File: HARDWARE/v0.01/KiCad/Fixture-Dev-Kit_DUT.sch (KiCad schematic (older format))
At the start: 33 parts, among them J34 Conn_01x20, J35 BAT, J36 CHIP4LH, J37 USB_OTG, J38 Conn_01x20, J39 VBUS, J40 VBUS, J41 B_D+, J42 D-TP's, J43 B_D-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

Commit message: adding datasheets
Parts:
- D13: value LED -> LNJP12X8ARA
- SW9: value SW_Push -> TL9210AF260Q
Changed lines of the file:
@@
 P 950 5250
 F 0 "SW9" H 1000 5350 50  0000 L CNN
-F 1 "SW_Push" H 950 5190 50  0000 C CNN
+F 1 "TL9210AF260Q" H 950 5190 50  0000 C CNN
 F 2 "" H 950 5450 50  0001 C CNN
 F 3 "" H 950 5450 50  0001 C CNN
@@
 P 2900 7200
 F 0 "D13" H 2900 7300 50  0000 C CNN
-F 1 "LED" H 2900 7100 50  0000 C CNN
+F 1 "LNJP12X8ARA" H 2900 7100 50  0000 C CNN
 F 2 "LEDs:LED_0805_HandSoldering" H 2900 7200 50  0001 C CNN
 F 3 "" H 2900 7200 50  0001 C CNN

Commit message: beginning pcb layout
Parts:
- added F2: 1206SFP300F, Fuse_Holders_and_Fuses:Fuse_SMD1206_HandSoldering, symbol Fuse
- added SW12: YSS-19-1202-N, symbol SW_Push_SPDT
- J36: footprint Pin_Headers:Pin_Header_Angled_2x20_Pitch2.54mm -> Pin_Headers:Pin_Header_Straight_2x20_Pitch2.54mm
- J52: footprint (none) -> Pin_Headers:Pin_Header_Straight_2x20_Pitch2.54mm
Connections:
- net DUT-CHG-IN: now reaches J36.2 (CHG-IN), J38.1 (Pin_1)
- net DUT-CHG-IN: now also J55.61 (USB_VBUS), J55.63 (USB_VBUS), J55.65 (USB_VBUS), J55.67 (USB_VBUS), J55.69 (USB_VBUS), J56.31 (Pin_31), J56.32 (Pin_32), J56.33 (Pin_33), J56.34 (Pin_34), J56.35 (Pin_35), F2.2
- new net: F2.1, SW12.3 (C)
- new net +5V: SW12.2 (B)
- no-connect marks 0 -> 1
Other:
- note added: "DUT-PWR\n"
- note added: "Sheet Connections"
- moved on the sheet: J42, J45, J46
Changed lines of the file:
@@
 $EndComp
 $Comp
-L GND #PWR043
+L GND #PWR047
 U 1 1 59EE39D0
 P 6700 4200
-F 0 "#PWR043" H 6700 3950 50  0001 C CNN
+F 0 "#PWR047" H 6700 3950 50  0001 C CNN
 F 1 "GND" H 6700 4050 50  0000 C CNN
 F 2 "" H 6700 4200 50  0001 C CNN
@@
 $EndComp
 $Comp
-L GND #PWR044
+L GND #PWR048
 U 1 1 59EE3CBF
 P 2850 4300
-F 0 "#PWR044" H 2850 4050 50  0001 C CNN
+F 0 "#PWR048" H 2850 4050 50  0001 C CNN
 F 1 "GND" H 2850 4150 50  0000 C CNN
 F 2 "" H 2850 4300 50  0001 C CNN
@@
 D-PWRON_SW
 $Comp
-L GND #PWR045
+L GND #PWR049
 U 1 1 59EE44BA
 P 950 5550
-F 0 "#PWR045" H 950 5300 50  0001 C CNN
+F 0 "#PWR049" H 950 5300 50  0001 C CNN
 F 1 "GND" H 950 5400 50  0000 C CNN
 F 2 "" H 950 5550 50  0001 C CNN
@@
 $EndComp
 $Comp
-L GND #PWR046
+L GND #PWR050
 U 1 1 59EE4976
 P 1400 6400
-F 0 "#PWR046" H 1400 6150 50  0001 C CNN
+F 0 "#PWR050" H 1400 6150 50  0001 C CNN
 F 1 "GND" H 1400 6250 50  0000 C CNN
 F 2 "" H 1400 6400 50  0001 C CNN
@@
 $EndComp
 $Comp
-L GND #PWR047
+L GND #PWR051
 U 1 1 59EE8E82
 P 7550 6100
-F 0 "#PWR047" H 7550 5850 50  0001 C CNN
+F 0 "#PWR051" H 7550 5850 50  0001 C CNN
 F 1 "GND" H 7550 5950 50  0000 C CNN
 F 2 "" H 7550 6100 50  0001 C CNN
@@
 $EndComp
 $Comp
-L GND #PWR048
+L GND #PWR052
 U 1 1 59EE9E75
 P 7550 2350
-F 0 "#PWR048" H 7550 2100 50  0001 C CNN
+F 0 "#PWR052" H 7550 2100 50  0001 C CNN
 F 1 "GND" H 7550 2200 50  0000 C CNN
 F 2 "" H 7550 2350 50  0001 C CNN
@@
 D-TS
 $Comp
-L GND #PWR049
+L GND #PWR053
 U 1 1 59EEAB1E
 P 1250 7500
-F 0 "#PWR049" H 1250 7250 50  0001 C CNN
+F 0 "#PWR053" H 1250 7250 50  0001 C CNN
 F 1 "GND" H 1250 7350 50  0000 C CNN
 F 2 "" H 1250 7500 50  0001 C CNN
@@
 $EndComp
 $Comp
-L GND #PWR050
+L GND #PWR054
 U 1 1 59EEBA3C
 P 2900 7450
-F 0 "#PWR050" H 2900 7200 50  0001 C CNN
+F 0 "#PWR054" H 2900 7200 50  0001 C CNN
 F 1 "GND" H 2900 7300 50  0000 C CNN
 F 2 "" H 2900 7450 50  0001 C CNN
@@
 F 0 "J36" H 1150 6250 60  0000 C CNN
 F 1 "CHIP4LH" H 1500 3900 60  0000 C CNN
-F 2 "Pin_Headers:Pin_Header_Angled_2x20_Pitch2.54mm" H 1800 4050 60  0001 C CNN
+F 2 "Pin_Headers:Pin_Header_Straight_2x20_Pitch2.54mm" H 1800 4050 60  0001 C CNN
 F 3 "" H 1800 4050 60  0001 C CNN
 	1    1700 4050
@@
 F 0 "J52" H 5050 6000 60  0000 C CNN
 F 1 "CHIP4RH" H 5300 3850 60  0000 C CNN
-F 2 "" H 5600 3950 60  0001 C CNN
+F 2 "Pin_Headers:Pin_Header_Straight_2x20_Pitch2.54mm" H 5600 3950 60  0001 C CNN
 F 3 "" H 5600 3950 60  0001 C CNN
 	1    5550 3950
@@
 $EndComp
 $Comp
-L GND #PWR051
+L GND #PWR055
 U 1 1 59EE623C
 P 2500 6050
-F 0 "#PWR051" H 2500 5800 50  0001 C CNN
+F 0 "#PWR055" H 2500 5800 50  0001 C CNN
 F 1 "GND" H 2500 5900 50  0000 C CNN
 F 2 "" H 2500 6050 50  0001 C CNN
@@
 $EndComp
 $Comp
-L GND #PWR052
+L GND #PWR056
 U 1 1 59EE91D1
 P 4650 6050
-F 0 "#PWR052" H 4650 5800 50  0001 C CNN
+F 0 "#PWR056" H 4650 5800 50  0001 C CNN
 F 1 "GND" H 4650 5900 50  0000 C CNN
 F 2 "" H 4650 6050 50  0001 C CNN
@@
 L Conn_01x01 J45
 U 1 1 59EEA0FF
-P 4450 6750
-F 0 "J45" H 4450 6850 50  0000 C CNN
-F 1 "UPDATE" H 4450 6650 50  0000 C CNN
-F 2 "Pin_Headers:Pin_Header_Angled_1x01_Pitch2.54mm" H 4450 6750 50  0001 C CNN
-F 3 "" H 4450 6750 50  0001 C CNN
-	1    4450 6750
+P 4400 6750
+F 0 "J45" H 4400 6850 50  0000 C CNN
+F 1 "UPDATE" H 4400 6650 50  0000 C CNN
+F 2 "Pin_Headers:Pin_Header_Angled_1x01_Pitch2.54mm" H 4400 6750 50  0001 C CNN
+F 3 "" H 4400 6750 50  0001 C CNN
+	1    4400 6750
 	1    0    0    -1
 $EndComp
@@
 L Conn_01x01 J46
 U 1 1 59EEA2FD
-P 4450 7050
-F 0 "J46" H 4450 7150 50  0000 C CNN
-F 1 "ANT--SELECT" H 4450 6950 50  0000 C CNN
-F 2 "Pin_Headers:Pin_Header_Angled_1x01_Pitch2.54mm" H 4450 7050 50  0001 C CNN
-F 3 "" H 4450 7050 50  0001 C CNN
-	1    4450 7050
+P 4400 7050
+F 0 "J46" H 4400 7150 50  0000 C CNN
+F 1 "ANT--SELECT" H 4400 6950 50  0000 C CNN
+F 2 "Pin_Headers:Pin_Header_Angled_1x01_Pitch2.54mm" H 4400 7050 50  0001 C CNN
+F 3 "" H 4400 7050 50  0001 C CNN
+	1    4400 7050
 	1    0    0    -1
 $EndComp
@@
 L Conn_01x02 J42
 U 1 1 59EEA72D
-P 3850 6950
-F 0 "J42" H 3850 7050 50  0000 C CNN
-F 1 "D-TP's" H 3850 6750 50  0000 C CNN
-F 2 "Pin_Headers:Pin_Header_Straight_1x02_Pitch2.54mm" H 3850 6950 50  0001 C CNN
-F 3 "" H 3850 6950 50  0001 C CNN
-	1    3850 6950
+P 3800 6950
+F 0 "J42" H 3800 7050 50  0000 C CNN
+F 1 "D-TP's" H 3800 6750 50  0000 C CNN
+F 2 "Pin_Headers:Pin_Header_Straight_1x02_Pitch2.54mm" H 3800 6950 50  0001 C CNN
+F 3 "" H 3800 6950 50  0001 C CNN
+	1    3800 6950
 	-1   0    0    1
 $EndComp
-Text Notes 3800 6450 0    98   ~ 0
+Text Notes 3750 6450 0    98   ~ 0
 DUT TPs
 Text Notes 550  800  0    197  ~ 0
@@
 	2500 2100 2850 2100
 Wire Wire Line
-	2800 2000 2500 2000
+	2500 2000 2900 2000
 Wire Wire Line
 	6700 2500 6700 4200
@@
 	9950 2550 9650 2550
 Wire Wire Line
-	9650 2650 9950 2650
+	9950 2650 9650 2650
 Wire Wire Line
 	9950 2750 9650 2750
 Wire Wire Line
-	9650 2850 9950 2850
+	9950 2850 9650 2850
 Wire Wire Line
 	9950 2950 9650 2950
 Wire Wire Line
-	10050 3050 9650 3050
+	9650 3050 10050 3050
 Wire Wire Line
 	9950 3150 9650 3150
@@
 	9950 5950 9650 5950
 Wire Wire Line
-	8000 5950 7550 5950
+	7550 5950 8000 5950
 Wire Wire Line
 	7700 5850 8000 5850
@@
 	7700 2650 8000 2650
 Wire Wire Line
-	8000 2550 7550 2550
-Wire Wire Line
-	9950 5550 9950 5950
+	7550 2550 8000 2550
+Wire Wire Line
+	9950 5550 9950 6250
 Connection ~ 9950 5650
 Connection ~ 9950 5750
@@
 Connection ~ 9950 3050
 Wire Wire Line
-	8000 2950 7550 2950
+	7550 2950 8000 2950
 Wire Wire Line
 	7700 2550 7700 2850
@@
 	4350 4700 5700 4700
 Wire Wire Line
-	4050 6850 4250 6850
-Wire Wire Line
-	4250 6850 4250 6750
-Wire Wire Line
-	4050 6950 4250 6950
-Wire Wire Line
-	4250 6950 4250 7050
-Wire Notes Line
-	3650 6300 5150 6300
-Wire Notes Line
-	5150 6300 5150 7300
-Wire Notes Line
-	5150 7300 3650 7300
-Wire Notes Line
-	3650 7300 3650 6300
+	4000 6850 4200 6850
+Wire Wire Line
+	4200 6850 4200 6750
+Wire Wire Line
+	4000 6950 4200 6950
+Wire Wire Line
+	4200 6950 4200 7050
+Wire Notes Line
+	3600 6300 5100 6300
+Wire Notes Line
+	5100 6300 5100 7300
+Wire Notes Line
+	5100 7300 3600 7300
+Wire Notes Line
+	3600 7300 3600 6300
 Wire Wire Line
 	950  2400 650  2400
@@
 Wire Notes Line
 	6850 1750 10400 1750
+Wire Notes Line
+	3600 6450 5100 6450
+Text Label 6050 6000 3    60   ~ 0
+DUT-CHG-IN
+Wire Wire Line
+	6050 5800 6050 6000
+$Comp
+L SW_Push_SPDT SW12
+U 1 1 59F29F6B
+P 6150 5300
+F 0 "SW12" H 6150 5470 50  0000 C CNN
+F 1 "YSS-19-1202-N" H 6150 5100 50  0000 C CNN
+F 2 "" H 6150 5300 50  0001 C CNN
+F 3 "" H 6150 5300 50  0001 C CNN
+	1    6150 5300
+	0    1    1    0
+$EndComp
+NoConn ~ 6250 5500
+$Comp
+L Fuse F2
+U 1 1 59F2A1E3
+P 6050 5650
+F 0 "F2" V 6130 5650 50  0000 C CNN
+F 1 "1206SFP300F" V 5975 5650 50  0000 C CNN
+F 2 "Fuse_Holders_and_Fuses:Fuse_SMD1206_HandSoldering" V 5980 5650 50  0001 C CNN
+F 3 "" H 6050 5650 50  0001 C CNN
+	1    6050 5650
+	1    0    0    -1
+$EndComp
+Text HLabel 850  1400 0    60   Input ~ 0
++5V
+Text Label 2900 2000 0    60   ~ 0
+DUT-CHG-IN
+Connection ~ 2800 2000
+Text Label 9950 6250 2    60   ~ 0
+DUT-CHG-IN
+Connection ~ 9950 5950
+Text Notes 5750 4700 0    98   ~ 0
+DUT-PWR\n
+Wire Notes Line
+	5750 4550 6500 4550
+Wire Notes Line
+	6500 4550 6500 6700
+Wire Notes Line
+	6500 6700 5750 6700
+Wire Notes Line
+	5750 6700 5750 4550
+Wire Notes Line
+	5750 4700 6500 4700
+$Comp
+L +5V #PWR057
+U 1 1 59F2C30C
+P 6150 5050
+F 0 "#PWR057" H 6150 4900 50  0001 C CNN
+F 1 "+5V" H 6150 5190 50  0000 C CNN
+F 2 "" H 6150 5050 50  0001 C CNN
+F 3 "" H 6150 5050 50  0001 C CNN
+	1    6150 5050
+	1    0    0    -1
+$EndComp
+Wire Wire Line
+	6150 5100 6150 5050
+$Comp
+L +5V #PWR058
+U 1 1 59F2C4FC
+P 950 1400
+F 0 "#PWR058" H 950 1250 50  0001 C CNN
+F 1 "+5V" H 950 1540 50  0000 C CNN
+F 2 "" H 950 1400 50  0001 C CNN
+F 3 "" H 950 1400 50  0001 C CNN
+	1    950  1400
+	0    1    1    0
+$EndComp
+Wire Wire Line
+	950  1400 850  1400
+Text Notes 600  1300 0    98   ~ 0
+Sheet Connections
+Wire Notes Line
+	550  1150 2000 1150
+Wire Notes Line
+	2000 1150 2000 1500
+Wire Notes Line
+	2000 1500 550  1500
+Wire Notes Line
+	550  1500 550  1150
 $EndSCHEMATC

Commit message: more PCB layout
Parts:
- J37: footprint (none) -> Connectors_USB:USB_Micro-B_Molex_47346-0001
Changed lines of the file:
@@
 F 0 "J37" H 2300 5900 50  0000 L CNN
 F 1 "USB_OTG" H 2300 5800 50  0000 L CNN
-F 2 "" H 2650 5400 50  0001 C CNN
+F 2 "Connectors_USB:USB_Micro-B_Molex_47346-0001" H 2650 5400 50  0001 C CNN
 F 3 "" H 2650 5400 50  0001 C CNN
 	1    2500 5450

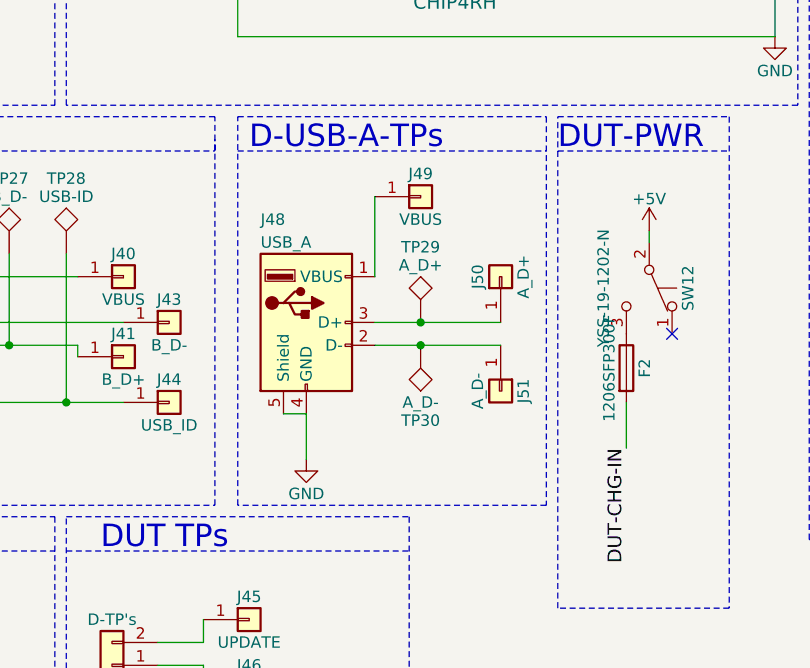
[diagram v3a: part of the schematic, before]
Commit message: adding datasheets and laying out PCB
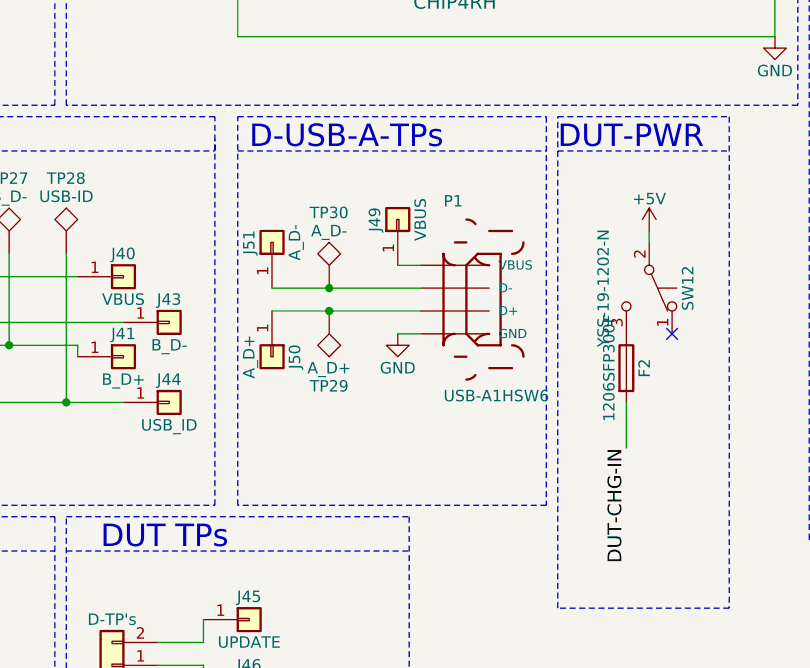
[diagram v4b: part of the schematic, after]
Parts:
- removed J48: USB_A, symbol USB_A
- added P1: USB-A1HSW6, symbol USB-A1HSW6
- F2: footprint Fuse_Holders_and_Fuses:Fuse_SMD1206_HandSoldering -> 1206:1206
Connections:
- net GND: now also P1.4 (GND)
- net at J49.1 (Pin_1): now also P1.1 (VBUS)
- net at J51.1 (Pin_1), TP30.1: now also P1.2 (D-)
- net at J50.1 (Pin_1), TP29.1: now also P1.3 (D+)
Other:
- moved on the sheet: J49, J50, J51, TP29, TP30
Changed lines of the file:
@@
 LIBS:valves
 LIBS:TCA6424ARGJR
+LIBS:USB-A1HSW6
 LIBS:Fixture-Dev-Kit-cache
 EELAYER 25 0
@@
 D-USBOTG-TPs\n
 $Comp
-L USB_A J48
-U 1 1 59EE80E3
-P 4650 5450
-F 0 "J48" H 4450 5900 50  0000 L CNN
-F 1 "USB_A" H 4450 5800 50  0000 L CNN
-F 2 "" H 4800 5400 50  0001 C CNN
-F 3 "" H 4800 5400 50  0001 C CNN
-	1    4650 5450
-	1    0    0    -1
-$EndComp
-$Comp
 L Conn_01x01 J50
 U 1 1 59EE8606
-P 5500 5250
-F 0 "J50" H 5500 5350 50  0000 C CNN
-F 1 "A_D+" H 5500 5150 50  0000 C CNN
-F 2 "Pin_Headers:Pin_Header_Angled_1x01_Pitch2.54mm" H 5500 5250 50  0001 C CNN
-F 3 "" H 5500 5250 50  0001 C CNN
-	1    5500 5250
-	0    -1   -1   0
+P 4500 5600
+F 0 "J50" H 4500 5700 50  0000 C CNN
+F 1 "A_D+" H 4500 5500 50  0000 C CNN
+F 2 "Pin_Headers:Pin_Header_Angled_1x01_Pitch2.54mm" H 4500 5600 50  0001 C CNN
+F 3 "" H 4500 5600 50  0001 C CNN
+	1    4500 5600
+	0    1    1    0
 $EndComp
 $Comp
 L Conn_01x01 J51
 U 1 1 59EE879F
-P 5500 5750
-F 0 "J51" H 5500 5850 50  0000 C CNN
-F 1 "A_D-" H 5500 5650 50  0000 C CNN
-F 2 "Pin_Headers:Pin_Header_Angled_1x01_Pitch2.54mm" H 5500 5750 50  0001 C CNN
-F 3 "" H 5500 5750 50  0001 C CNN
-	1    5500 5750
-	0    1    1    0
+P 4500 5100
+F 0 "J51" H 4500 5200 50  0000 C CNN
+F 1 "A_D-" H 4500 5000 50  0000 C CNN
+F 2 "Pin_Headers:Pin_Header_Angled_1x01_Pitch2.54mm" H 4500 5100 50  0001 C CNN
+F 3 "" H 4500 5100 50  0001 C CNN
+	1    4500 5100
+	0    -1   -1   0
 $EndComp
 $Comp
 L TEST TP30
 U 1 1 59EE8980
-P 5150 5550
-F 0 "TP30" H 5150 5850 50  0000 C BNN
-F 1 "A_D-" H 5150 5800 50  0000 C CNN
-F 2 "TestPoint:TestPoint" H 5150 5550 50  0001 C CNN
-F 3 "" H 5150 5550 50  0001 C CNN
-	1    5150 5550
-	-1   0    0    1
+P 4750 5300
+F 0 "TP30" H 4750 5600 50  0000 C BNN
+F 1 "A_D-" H 4750 5550 50  0000 C CNN
+F 2 "TestPoint:TestPoint" H 4750 5300 50  0001 C CNN
+F 3 "" H 4750 5300 50  0001 C CNN
+	1    4750 5300
+	1    0    0    -1
 $EndComp
 $Comp
 L TEST TP29
 U 1 1 59EE8A8A
-P 5150 5450
-F 0 "TP29" H 5150 5750 50  0000 C BNN
-F 1 "A_D+" H 5150 5700 50  0000 C CNN
-F 2 "TestPoint:TestPoint" H 5150 5450 50  0001 C CNN
-F 3 "" H 5150 5450 50  0001 C CNN
-	1    5150 5450
-	1    0    0    -1
+P 4750 5400
+F 0 "TP29" H 4750 5700 50  0000 C BNN
+F 1 "A_D+" H 4750 5650 50  0000 C CNN
+F 2 "TestPoint:TestPoint" H 4750 5400 50  0001 C CNN
+F 3 "" H 4750 5400 50  0001 C CNN
+	1    4750 5400
+	-1   0    0    1
 $EndComp
 $Comp
 L GND #PWR056
 U 1 1 59EE91D1
-P 4650 6050
-F 0 "#PWR056" H 4650 5800 50  0001 C CNN
-F 1 "GND" H 4650 5900 50  0000 C CNN
-F 2 "" H 4650 6050 50  0001 C CNN
-F 3 "" H 4650 6050 50  0001 C CNN
-	1    4650 6050
+P 5050 5500
+F 0 "#PWR056" H 5050 5250 50  0001 C CNN
+F 1 "GND" H 5050 5350 50  0000 C CNN
+F 2 "" H 5050 5500 50  0001 C CNN
+F 3 "" H 5050 5500 50  0001 C CNN
+	1    5050 5500
 	1    0    0    -1
 $EndComp
@@
 L Conn_01x01 J49
 U 1 1 59F0CD26
-P 5150 4900
-F 0 "J49" H 5150 5000 50  0000 C CNN
-F 1 "VBUS" H 5150 4800 50  0000 C CNN
-F 2 "Pin_Headers:Pin_Header_Angled_1x01_Pitch2.54mm" H 5150 4900 50  0001 C CNN
-F 3 "" H 5150 4900 50  0001 C CNN
-	1    5150 4900
-	1    0    0    -1
+P 5050 5000
+F 0 "J49" H 5050 5100 50  0000 C CNN
+F 1 "VBUS" H 5050 4900 50  0000 C CNN
+F 2 "Pin_Headers:Pin_Header_Angled_1x01_Pitch2.54mm" H 5050 5000 50  0001 C CNN
+F 3 "" H 5050 5000 50  0001 C CNN
+	1    5050 5000
+	0    -1   -1   0
 $EndComp
 Text Notes 13150 2550 0    197  ~ 0
@@
 Wire Notes Line
 	4250 4700 4250 4650
-Wire Wire Line
-	4950 5450 5500 5450
-Connection ~ 5150 5450
-Wire Wire Line
-	4950 5550 5500 5550
-Connection ~ 5150 5550
-Wire Wire Line
-	4550 5850 4650 5850
-Wire Wire Line
-	4650 5850 4650 6050
 Wire Notes Line
 	4350 4550 5700 4550
@@
 	3000 6050 3000 5250
 Connection ~ 3000 5250
-Wire Wire Line
-	4950 4900 4950 5250
 Wire Notes Line
 	6850 6400 10400 6400
@@
 F 0 "F2" V 6130 5650 50  0000 C CNN
 F 1 "1206SFP300F" V 5975 5650 50  0000 C CNN
-F 2 "Fuse_Holders_and_Fuses:Fuse_SMD1206_HandSoldering" V 5980 5650 50  0001 C CNN
+F 2 "1206:1206" V 5980 5650 50  0001 C CNN
 F 3 "" H 6050 5650 50  0001 C CNN
 	1    6050 5650
@@
 Wire Notes Line
 	550  1500 550  1150
+$Comp
+L USB-A1HSW6 P1
+U 1 1 59F40222
+P 5350 5400
+F 0 "P1" H 5250 5851 50  0000 L BNN
+F 1 "USB-A1HSW6" H 5250 4999 50  0000 L BNN
+F 2 "" H 5350 5400 50  0001 L BNN
+F 3 "On Shore Technology" H 5350 5400 50  0001 L BNN
+F 4 "None" H 5350 5400 50  0001 L BNN "Package"
+F 5 "Conn Usb Type a r/a White" H 5350 5400 50  0001 L BNN "Description"
+F 6 "Good" H 5350 5400 50  0001 L BNN "Availability"
+F 7 "USB-A1HSW6" H 5350 5400 50  0001 L BNN "MP"
+F 8 "0.31 USD" H 5350 5400 50  0001 L BNN "Price"
+	1    5350 5400
+	1    0    0    -1
+$EndComp
+Wire Wire Line
+	5050 5200 5150 5200
+Wire Wire Line
+	5150 5500 5050 5500
+Wire Wire Line
+	4500 5400 5150 5400
+Connection ~ 4750 5400
+Wire Wire Line
+	4500 5300 5150 5300
+Connection ~ 4750 5300
 $EndSCHEMATC
